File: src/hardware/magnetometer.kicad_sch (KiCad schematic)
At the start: 4 parts

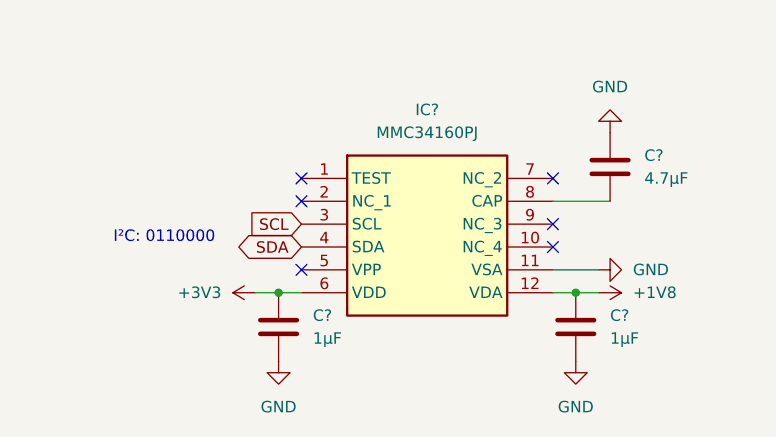
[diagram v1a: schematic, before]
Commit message: Replaced schematics, 3d models and footprints. Added vibration motor.
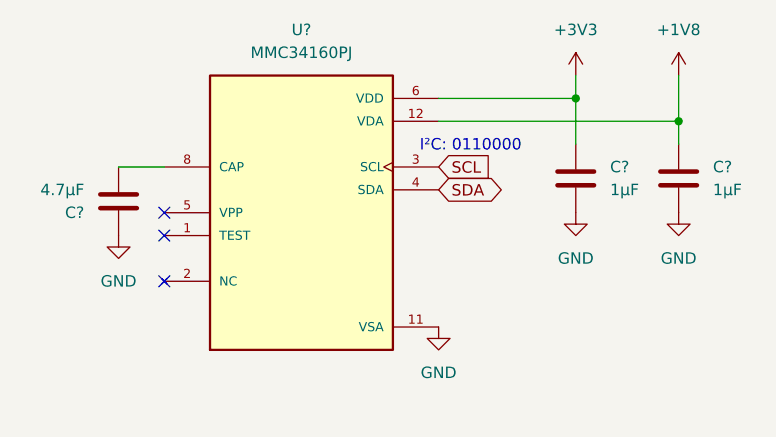
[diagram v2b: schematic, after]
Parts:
- removed IC?: MMC34160PJ, MMC34160PJ, symbol MMC34160PJ:MMC34160PJ
- added U?: MMC34160PJ, MMC34160PJ:XDCR_MMC34160PJ, symbol MMC34160PJ:MMC34160PJ
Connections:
- net +1V8: now also U?.12 (VDA)
- net +3V3: now also U?.6 (VDD)
- net GND: now also U?.11 (VSA)
- net SCL: now also U?.3 (SCL)
- net SDA: now also U?.4 (SDA)
- net at C?.1: now also U?.8 (CAP)
- new net: U?.10 (NC), U?.2 (NC), U?.7 (NC), U?.9 (NC)
- no-connect marks 6 -> 3
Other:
- moved on the sheet: C?

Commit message: Added LoRa
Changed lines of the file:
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@@
 		(fields_autoplaced yes)
 		(property "Reference" "C?"
-			(at 114.3 100.3301 0)
+			(at 114.3 97.7899 0)
 			(effects
 				(font
@@
 		)
 		(property "Value" "4.7µF"
-			(at 114.3 97.7901 0)
+			(at 114.3 100.3299 0)
 			(effects
 				(font

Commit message: Selected GPIO
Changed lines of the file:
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@@
 		)
 		(property "Value" "+3V3"
-			(at 168.91 80.01 0)
-			(effects
-				(font
-					(size 1.27 1.27)
-				)
+			(at 171.45 83.8199 0)
+			(effects
+				(font
+					(size 1.27 1.27)
+				)
+				(justify left)
 			)
 		)
@@
 		)
 		(property "Value" "+1V8"
-			(at 180.34 80.01 0)
-			(effects
-				(font
-					(size 1.27 1.27)
-				)
+			(at 182.88 83.8199 0)
+			(effects
+				(font
+					(size 1.27 1.27)
+				)
+				(justify left)
 			)
 		)
@@
 		)
 		(property "Value" "GND"
-			(at 153.67 118.11 0)
-			(effects
-				(font
-					(size 1.27 1.27)
-				)
-			)
-		)
+			(at 156.21 114.2999 0)
+			(effects
+				(font
+					(size 1.27 1.27)
+				)
+				(justify left)
+			)
+		)

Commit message: Cleanup & Fixes; Added footprints; Removed Light sensors
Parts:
- C53, C54, C55: renamed from C?; footprint (none) -> Capacitor_SMD:C_0603_1608Metric
- U17: renamed from U?; footprint MMC34160PJ:XDCR_MMC34160PJ -> Project:XDCR_MMC34160PJ
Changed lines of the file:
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@@
 		(dnp no)
 		(fields_autoplaced yes)
-		(property "Reference" "C?"
+		(property "Reference" "C53"
 			(at 114.3 97.7899 0)
 			(effects
@@
 			)
 		)
-		(property "Footprint" ""
+		(property "Footprint" "Capacitor_SMD:C_0603_1608Metric"
 			(at 119.0752 102.87 0)
 			(effects
@@
 			(project "raywatch"
 				(path "/7b654ee8-2a53-4d39-8b7d-32c7bb3cb0ed/9d8e2113-86ca-4807-a845-38f03d871655"
-					(reference "C?")
+					(reference "C53")
 					(unit 1)
 				)
@@
 		(dnp no)
 		(fields_autoplaced yes)
-		(property "Reference" "#PWR0302"
+		(property "Reference" "#PWR0311"
 			(at 168.91 88.9 0)
 			(effects
@@
 		)
 		(property "Value" "+3V3"
-			(at 171.45 83.8199 0)
-			(effects
-				(font
-					(size 1.27 1.27)
-				)
-				(justify left)
+			(at 168.91 80.01 0)
+			(effects
+				(font
+					(size 1.27 1.27)
+				)
 			)
 		)
@@
 			(project "raywatch"
 				(path "/7b654ee8-2a53-4d39-8b7d-32c7bb3cb0ed/9d8e2113-86ca-4807-a845-38f03d871655"
-					(reference "#PWR0302")
+					(reference "#PWR0311")
 					(unit 1)
 				)
@@
 		(dnp no)
 		(fields_autoplaced yes)
-		(property "Reference" "#PWR0305"
+		(property "Reference" "#PWR0309"
 			(at 118.11 109.22 0)
 			(effects
@@
 			(project "raywatch"
 				(path "/7b654ee8-2a53-4d39-8b7d-32c7bb3cb0ed/9d8e2113-86ca-4807-a845-38f03d871655"
-					(reference "#PWR0305")
+					(reference "#PWR0309")
 					(unit 1)
 				)
@@
 		(dnp no)
 		(fields_autoplaced yes)
-		(property "Reference" "#PWR0301"
+		(property "Reference" "#PWR0313"
 			(at 180.34 88.9 0)
 			(effects
@@
 		)
 		(property "Value" "+1V8"
-			(at 182.88 83.8199 0)
-			(effects
-				(font
-					(size 1.27 1.27)
-				)
-				(justify left)
+			(at 180.34 80.01 0)
+			(effects
+				(font
+					(size 1.27 1.27)
+				)
 			)
 		)
@@
 			(project "raywatch"
 				(path "/7b654ee8-2a53-4d39-8b7d-32c7bb3cb0ed/9d8e2113-86ca-4807-a845-38f03d871655"
-					(reference "#PWR0301")
+					(reference "#PWR0313")
 					(unit 1)
 				)
@@
 		(dnp no)
 		(fields_autoplaced yes)
-		(property "Reference" "#PWR0306"
+		(property "Reference" "#PWR0310"
 			(at 153.67 119.38 0)
 			(effects
@@
 		)
 		(property "Value" "GND"
-			(at 156.21 114.2999 0)
-			(effects
-				(font
-					(size 1.27 1.27)
-				)
-				(justify left)
+			(at 153.67 118.11 0)
+			(effects
+				(font
+					(size 1.27 1.27)
+				)
 			)
 		)
@@
 			(project "raywatch"
 				(path "/7b654ee8-2a53-4d39-8b7d-32c7bb3cb0ed/9d8e2113-86ca-4807-a845-38f03d871655"
-					(reference "#PWR0306")
+					(reference "#PWR0310")
 					(unit 1)
 				)
@@
 		(dnp no)
 		(fields_autoplaced yes)
-		(property "Reference" "#PWR0303"
+		(property "Reference" "#PWR0312"
 			(at 168.91 106.68 0)
 			(effects
@@
 			(project "raywatch"
 				(path "/7b654ee8-2a53-4d39-8b7d-32c7bb3cb0ed/9d8e2113-86ca-4807-a845-38f03d871655"
-					(reference "#PWR0303")
+					(reference "#PWR0312")
 					(unit 1)
 				)
@@
 		(dnp no)
 		(fields_autoplaced yes)
-		(property "Reference" "C?"
+		(property "Reference" "C54"
 			(at 172.72 95.2499 0)
 			(effects
@@
 			)
 		)
-		(property "Footprint" ""
+		(property "Footprint" "Capacitor_SMD:C_0603_1608Metric"
 			(at 169.8752 100.33 0)
 			(effects
@@
 			(project "raywatch"
 				(path "/7b654ee8-2a53-4d39-8b7d-32c7bb3cb0ed/9d8e2113-86ca-4807-a845-38f03d871655"
-					(reference "C?")
+					(reference "C54")
 					(unit 1)
 				)
@@
 		(dnp no)
 		(fields_autoplaced yes)
-		(property "Reference" "#PWR0304"
+		(property "Reference" "#PWR0314"
 			(at 180.34 106.68 0)
 			(effects
@@
 			(project "raywatch"
 				(path "/7b654ee8-2a53-4d39-8b7d-32c7bb3cb0ed/9d8e2113-86ca-4807-a845-38f03d871655"
-					(reference "#PWR0304")
+					(reference "#PWR0314")
 					(unit 1)
 				)
@@
 		(dnp no)
 		(fields_autoplaced yes)
-		(property "Reference" "U?"
+		(property "Reference" "U17"
 			(at 138.43 80.01 0)
 			(effects
@@
 			)
 		)
-		(property "Footprint" "MMC34160PJ:XDCR_MMC34160PJ"
+		(property "Footprint" "Project:XDCR_MMC34160PJ"
 			(at 138.43 100.33 0)
 			(effects
@@
 			(project "raywatch"
 				(path "/7b654ee8-2a53-4d39-8b7d-32c7bb3cb0ed/9d8e2113-86ca-4807-a845-38f03d871655"
-					(reference "U?")
+					(reference "U17")
 					(unit 1)
 				)
@@
 		(dnp no)
 		(fields_autoplaced yes)
-		(property "Reference" "C?"
+		(property "Reference" "C55"
 			(at 184.15 95.2499 0)
 			(effects
@@
 			)
 		)
-		(property "Footprint" ""
+		(property "Footprint" "Capacitor_SMD:C_0603_1608Metric"
 			(at 181.3052 100.33 0)
 			(effects
@@
 			(project "raywatch"
 				(path "/7b654ee8-2a53-4d39-8b7d-32c7bb3cb0ed/9d8e2113-86ca-4807-a845-38f03d871655"
-					(reference "C?")
-					(unit 1)
-				)
+					(reference "C55")
+					(unit 1)
+				)

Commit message: Cleanup & Fixes; Changed GPIO; Added Camera; Added Microphone
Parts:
- renumbered C53 to C51, C54 to C52, C55 to C53
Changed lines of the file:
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@@
 		(dnp no)
 		(fields_autoplaced yes)
-		(property "Reference" "C53"
+		(property "Reference" "C51"
 			(at 114.3 97.7899 0)
 			(effects
@@
 			(project "raywatch"
 				(path "/7b654ee8-2a53-4d39-8b7d-32c7bb3cb0ed/9d8e2113-86ca-4807-a845-38f03d871655"
-					(reference "C53")
+					(reference "C51")
 					(unit 1)
 				)
@@
 		(dnp no)
 		(fields_autoplaced yes)
-		(property "Reference" "#PWR0311"
+		(property "Reference" "#PWR0307"
 			(at 168.91 88.9 0)
 			(effects
@@
 			(project "raywatch"
 				(path "/7b654ee8-2a53-4d39-8b7d-32c7bb3cb0ed/9d8e2113-86ca-4807-a845-38f03d871655"
-					(reference "#PWR0311")
+					(reference "#PWR0307")
 					(unit 1)
 				)
@@
 		(dnp no)
 		(fields_autoplaced yes)
-		(property "Reference" "#PWR0309"
+		(property "Reference" "#PWR0305"
 			(at 118.11 109.22 0)
 			(effects
@@
 			(project "raywatch"
 				(path "/7b654ee8-2a53-4d39-8b7d-32c7bb3cb0ed/9d8e2113-86ca-4807-a845-38f03d871655"
-					(reference "#PWR0309")
+					(reference "#PWR0305")
 					(unit 1)
 				)
@@
 		(dnp no)
 		(fields_autoplaced yes)
-		(property "Reference" "#PWR0313"
+		(property "Reference" "#PWR0309"
 			(at 180.34 88.9 0)
 			(effects
@@
 			(project "raywatch"
 				(path "/7b654ee8-2a53-4d39-8b7d-32c7bb3cb0ed/9d8e2113-86ca-4807-a845-38f03d871655"
-					(reference "#PWR0313")
+					(reference "#PWR0309")
 					(unit 1)
 				)
@@
 		(dnp no)
 		(fields_autoplaced yes)
-		(property "Reference" "#PWR0310"
+		(property "Reference" "#PWR0306"
 			(at 153.67 119.38 0)
 			(effects
@@
 			(project "raywatch"
 				(path "/7b654ee8-2a53-4d39-8b7d-32c7bb3cb0ed/9d8e2113-86ca-4807-a845-38f03d871655"
-					(reference "#PWR0310")
+					(reference "#PWR0306")
 					(unit 1)
 				)
@@
 		(dnp no)
 		(fields_autoplaced yes)
-		(property "Reference" "#PWR0312"
+		(property "Reference" "#PWR0308"
 			(at 168.91 106.68 0)
 			(effects
@@
 			(project "raywatch"
 				(path "/7b654ee8-2a53-4d39-8b7d-32c7bb3cb0ed/9d8e2113-86ca-4807-a845-38f03d871655"
-					(reference "#PWR0312")
+					(reference "#PWR0308")
 					(unit 1)
 				)
@@
 		(dnp no)
 		(fields_autoplaced yes)
-		(property "Reference" "C54"
+		(property "Reference" "C52"
 			(at 172.72 95.2499 0)
 			(effects
@@
 			(project "raywatch"
 				(path "/7b654ee8-2a53-4d39-8b7d-32c7bb3cb0ed/9d8e2113-86ca-4807-a845-38f03d871655"
-					(reference "C54")
+					(reference "C52")
 					(unit 1)
 				)
@@
 		(dnp no)
 		(fields_autoplaced yes)
-		(property "Reference" "#PWR0314"
+		(property "Reference" "#PWR0310"
 			(at 180.34 106.68 0)
 			(effects
@@
 			(project "raywatch"
 				(path "/7b654ee8-2a53-4d39-8b7d-32c7bb3cb0ed/9d8e2113-86ca-4807-a845-38f03d871655"
-					(reference "#PWR0314")
+					(reference "#PWR0310")
 					(unit 1)
 				)
@@
 		(dnp no)
 		(fields_autoplaced yes)
-		(property "Reference" "C55"
+		(property "Reference" "C53"
 			(at 184.15 95.2499 0)
 			(effects
@@
 			(project "raywatch"
 				(path "/7b654ee8-2a53-4d39-8b7d-32c7bb3cb0ed/9d8e2113-86ca-4807-a845-38f03d871655"
-					(reference "C55")
-					(unit 1)
-				)
+					(reference "C53")
+					(unit 1)
+				)

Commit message: Add Light Sensor and Proximity & Gesture Sensor; Changed GPIO
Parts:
- renumbered U17 to U18
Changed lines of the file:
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@@
 		(dnp no)
 		(fields_autoplaced yes)
-		(property "Reference" "#PWR0307"
+		(property "Reference" "#PWR0311"
 			(at 168.91 88.9 0)
 			(effects
@@
 			(project "raywatch"
 				(path "/7b654ee8-2a53-4d39-8b7d-32c7bb3cb0ed/9d8e2113-86ca-4807-a845-38f03d871655"
-					(reference "#PWR0307")
+					(reference "#PWR0311")
 					(unit 1)
 				)
@@
 		(dnp no)
 		(fields_autoplaced yes)
-		(property "Reference" "#PWR0305"
+		(property "Reference" "#PWR0309"
 			(at 118.11 109.22 0)
 			(effects
@@
 			(project "raywatch"
 				(path "/7b654ee8-2a53-4d39-8b7d-32c7bb3cb0ed/9d8e2113-86ca-4807-a845-38f03d871655"
-					(reference "#PWR0305")
+					(reference "#PWR0309")
 					(unit 1)
 				)
@@
 		(dnp no)
 		(fields_autoplaced yes)
-		(property "Reference" "#PWR0309"
+		(property "Reference" "#PWR0313"
 			(at 180.34 88.9 0)
 			(effects
@@
 			(project "raywatch"
 				(path "/7b654ee8-2a53-4d39-8b7d-32c7bb3cb0ed/9d8e2113-86ca-4807-a845-38f03d871655"
-					(reference "#PWR0309")
+					(reference "#PWR0313")
 					(unit 1)
 				)
@@
 		(dnp no)
 		(fields_autoplaced yes)
-		(property "Reference" "#PWR0306"
+		(property "Reference" "#PWR0310"
 			(at 153.67 119.38 0)
 			(effects
@@
 			(project "raywatch"
 				(path "/7b654ee8-2a53-4d39-8b7d-32c7bb3cb0ed/9d8e2113-86ca-4807-a845-38f03d871655"
-					(reference "#PWR0306")
+					(reference "#PWR0310")
 					(unit 1)
 				)
@@
 		(dnp no)
 		(fields_autoplaced yes)
-		(property "Reference" "#PWR0308"
+		(property "Reference" "#PWR0312"
 			(at 168.91 106.68 0)
 			(effects
@@
 			(project "raywatch"
 				(path "/7b654ee8-2a53-4d39-8b7d-32c7bb3cb0ed/9d8e2113-86ca-4807-a845-38f03d871655"
-					(reference "#PWR0308")
+					(reference "#PWR0312")
 					(unit 1)
 				)
@@
 		(dnp no)
 		(fields_autoplaced yes)
-		(property "Reference" "#PWR0310"
+		(property "Reference" "#PWR0314"
 			(at 180.34 106.68 0)
 			(effects
@@
 			(project "raywatch"
 				(path "/7b654ee8-2a53-4d39-8b7d-32c7bb3cb0ed/9d8e2113-86ca-4807-a845-38f03d871655"
-					(reference "#PWR0310")
+					(reference "#PWR0314")
 					(unit 1)
 				)
@@
 		(dnp no)
 		(fields_autoplaced yes)
-		(property "Reference" "U17"
+		(property "Reference" "U18"
 			(at 138.43 80.01 0)
 			(effects
@@
 			(project "raywatch"
 				(path "/7b654ee8-2a53-4d39-8b7d-32c7bb3cb0ed/9d8e2113-86ca-4807-a845-38f03d871655"
-					(reference "U17")
-					(unit 1)
-				)
+					(reference "U18")
+					(unit 1)
+				)
